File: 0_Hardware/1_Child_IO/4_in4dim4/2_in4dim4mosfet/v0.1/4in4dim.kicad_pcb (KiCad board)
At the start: 2 copper layers, 100.1 x 86.4 mm, 79 parts, among them IC1 TLP290, J1 RJ45, J2 RJ45, P1 CONN_5, P110 CONN_2, P120 CONN_2, P130 CONN_2, P140 CONN_2, P2 CONN_2, P3 CONN_8X2, Q1 SPP20N60C3, Q2 SPP20N60C3, Q3 SPP20N60C3, Q4 SPP20N60C3, U2 LTV847, U3 LTV847

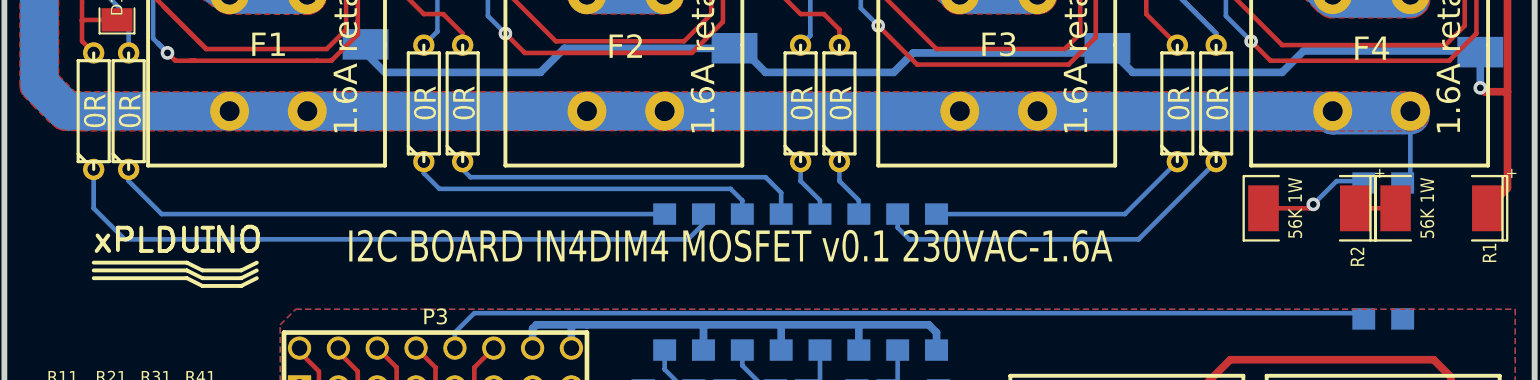
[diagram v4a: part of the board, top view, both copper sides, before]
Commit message: IN4DIM4: remplacement empreinte PNP par SOT-23 standard
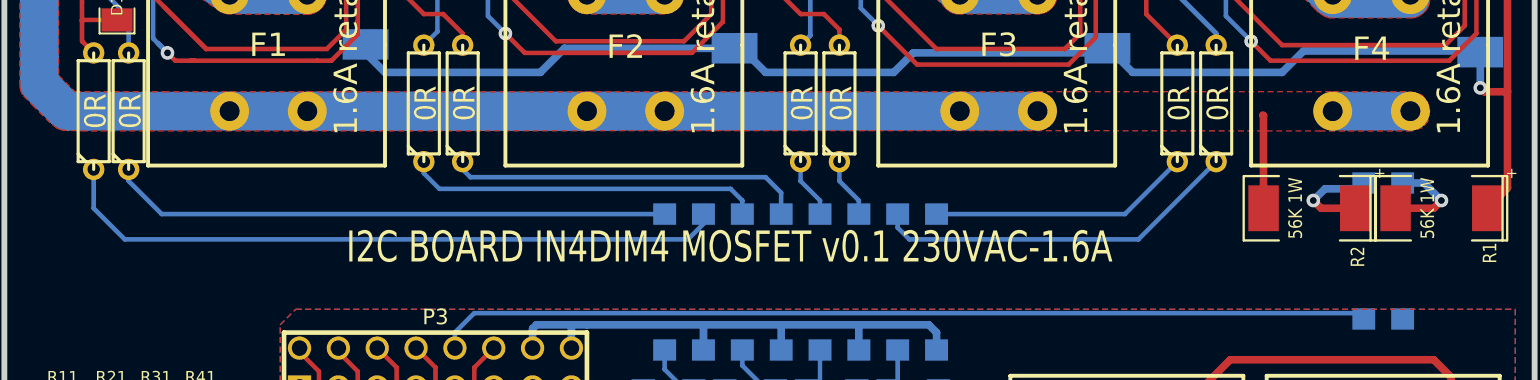
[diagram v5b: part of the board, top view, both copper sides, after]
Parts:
- removed logo_xplduino: VAL**, logo_xplduino
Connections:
- IC1 pad 1: N-0000027 -> N-0000026
- IC1 pad 2: L -> N-0000025
- R1 pad 2: N-0000026 -> N-0000025
- R2 pad 2: N-0000027 -> L
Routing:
- net L: track 158.2 -> 135.5 mm
- net N-0000027: track 7.80 -> 0.00 mm, vias 1 -> 0
- net N-0000025: track 0.00 -> 6.22 mm, vias 0 -> 1
- net N-0000026: track 2.64 -> 6.73 mm, vias 0 -> 1

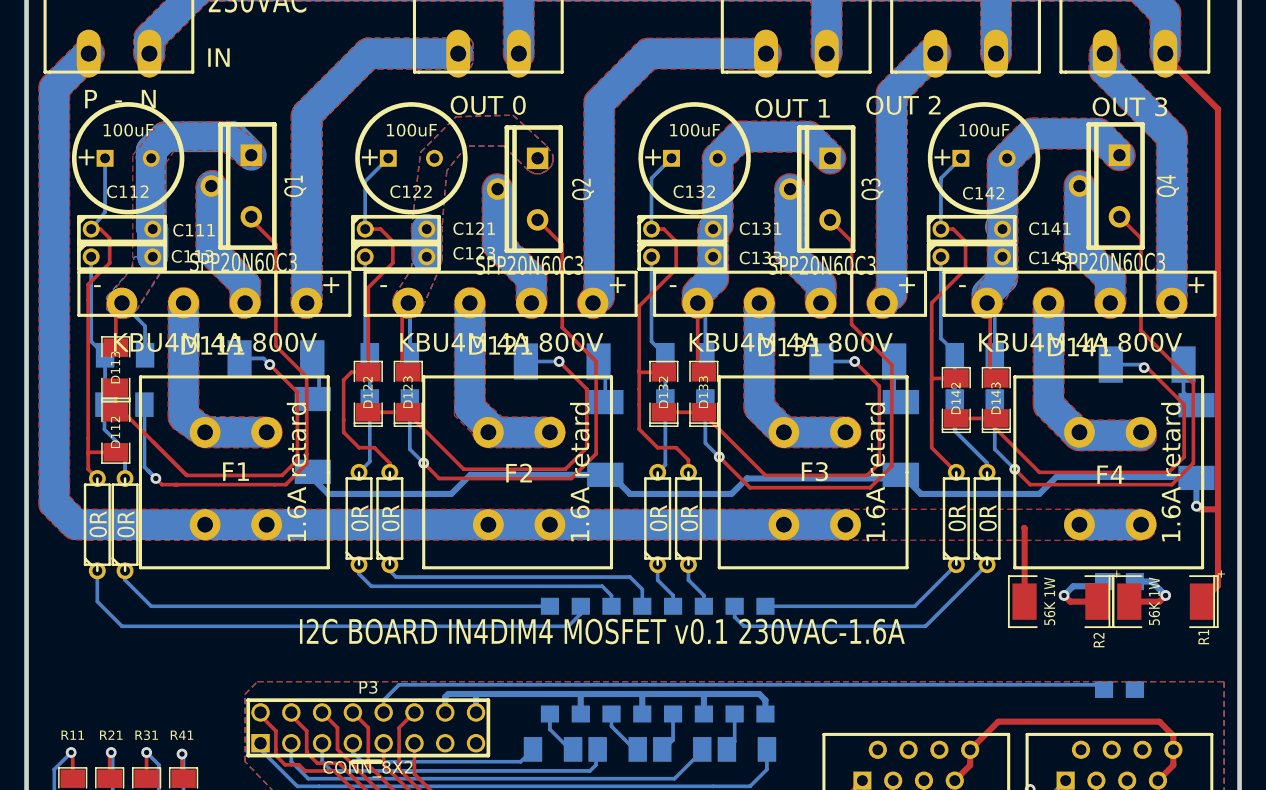
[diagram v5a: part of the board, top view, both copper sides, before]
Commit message: echange format resistance nulle (RPx) pour plus grand longueur
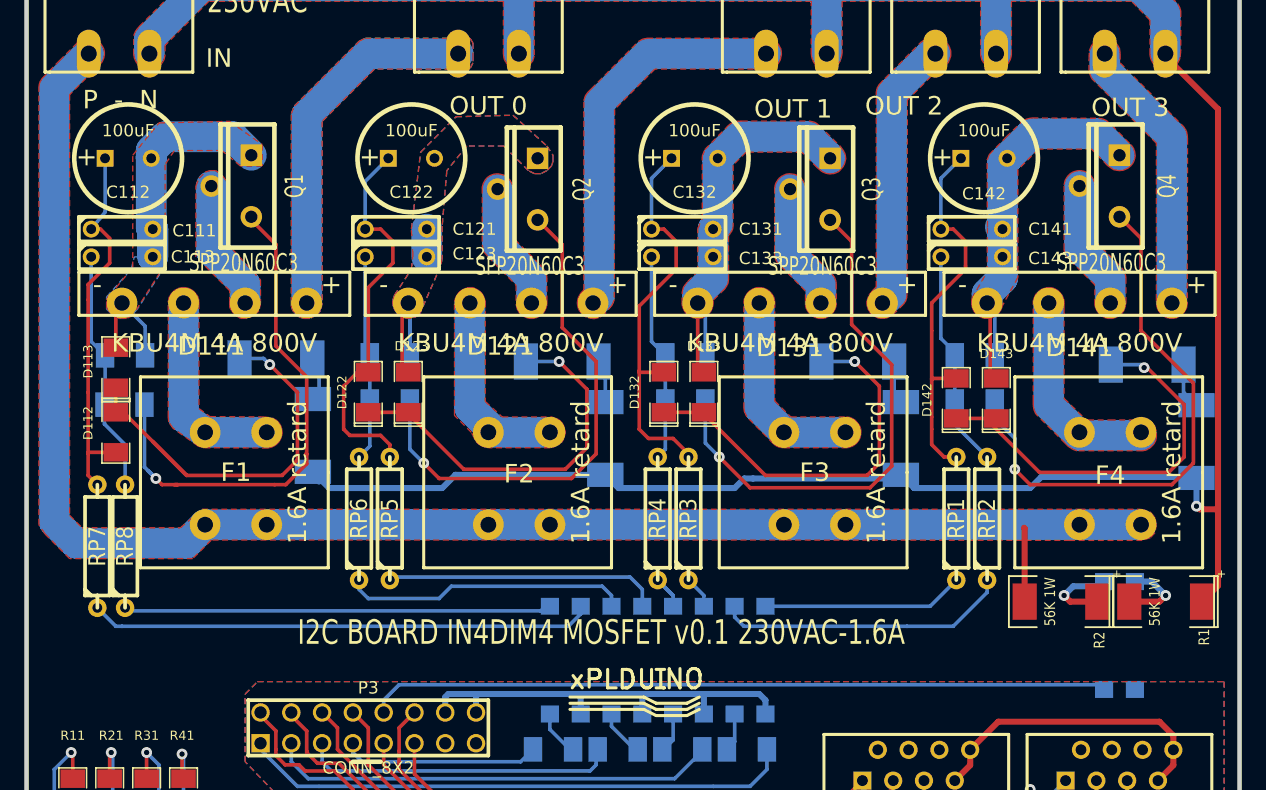
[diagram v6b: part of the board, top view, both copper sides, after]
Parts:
- added logo_xplduino: VAL**, logo_xplduino, F.Cu at (231.8, 134.6)
- RP1, RP2, RP3, RP4, RP5, RP6, RP7, RP8: footprint R3 -> R4
- moved RP7 1.78 mm to (187.5, 121.9)
- moved RP8 1.78 mm to (189.7, 121.9)
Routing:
- net L: track 135.5 -> 157.0 mm
- net OUT3_B: track 26.3 -> 17.6 mm
- net N-000009: track 44.3 -> 41.6 mm
- net OUT2_B: track 19.4 -> 17.2 mm
- net N: track 242.0 -> 240.5 mm
- net N-000008: track 36.7 -> 35.3 mm
- net OUT1_B: track 18.3 -> 17.0 mm
- net N-0000010: track 3.96 -> 2.69 mm
- net N-0000015: track 23.4 -> 22.1 mm
- net OUT2_A: track 34.0 -> 32.9 mm
- net OUT1_A: track 33.2 -> 32.4 mm
- net OUT3_A: track 32.2 -> 31.5 mm
- net N-0000012: track 17.2 -> 16.6 mm
- net N-0000013: track 3.96 -> 4.48 mm
- net OUT0_B: track 19.5 -> 20.0 mm
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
